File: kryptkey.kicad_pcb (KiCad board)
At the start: 2 copper layers, 34 parts, among them J1 Conn_01x04_Pin, J2 Conn_01x04_Pin, P1 USB_C_Plug, SW4 SW_SPDT, U1 AMS1117-3.3, U2 STM32F103C8T6, Y1 16MHz

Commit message: worked on board layout
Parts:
- removed P1: USB_C_Plug, Connector_USB:USB_C_Plug_Molex_105444
- removed the R2 at (159.2, 77.5)
- added P2: USB_C_Plug_USB2.0, Connector_USB:USB_C_Plug_JAE_DX07P024AJ1, B.Cu at (155.6, 85.0)
- added SW1: SW_Push, Button_Switch_SMD:SW_SPST_B3U-1000P, F.Cu at (145.7, 118.2)
- added SW2: SW_Push, Button_Switch_SMD:SW_SPST_B3U-1000P, F.Cu at (155.7, 117.8)
- added SW3: SW_Push, Button_Switch_SMD:SW_SPST_B3U-1000P, F.Cu at (164.2, 118.0)
- FB1: footprint Inductor_SMD:L_12x12mm_H8mm -> Inductor_SMD:L_0603_1608Metric
- H1, H2, H3, H4: footprint MountingHole:MountingHole_2.5mm -> MountingHole:MountingHole_2.7mm_M2.5
- J2: footprint Connector_PinHeader_2.54mm:PinHeader_1x04_P2.54mm_Vertical -> Connector_PinHeader_2.54mm:PinHeader_1x04_P2.54mm_Horizontal
- SW4: footprint Button_Switch_THT:SW_E-Switch_EG1224_SPDT_Angled -> Button_Switch_THT:SW_E-Switch_EG1271_SPDT
- moved H4 58.8 mm to (165.0, 113.5)
- moved H3 58.6 mm to (165.6, 90.7)
- moved D1 51.0 mm to (167.9, 108.2)
- moved SW4 49.5 mm to (158.1, 115.0), turned to 180 degrees
- moved H2 40.7 mm to (144.8, 113.5)
- moved H1 39.2 mm to (144.8, 90.7)
- moved U1 37.8 mm to (165.2, 102.8)
- moved C10 31.7 mm to (158.1, 108.4), turned to 180 degrees
- moved C13 31.6 mm to (154.1, 109.1), turned to 90 degrees
- moved Y1 28.2 mm to (146.9, 99.1), turned to 180 degrees
- moved R5 27.6 mm to (161.5, 85.8), turned to 180 degrees
- moved C4 26.5 mm to (147.1, 105.2), turned to 180 degrees
- moved R3 23.9 mm to (164.4, 108.3)
- moved R4 22.8 mm to (161.2, 114.6), turned to 90 degrees
- moved U2 21.6 mm to (155.5, 101.1)
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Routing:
- added copper zone on B.Cu, net GND
- added copper zone on F.Cu, net GND
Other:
- board outline added: 30 x 36 mm

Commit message: worked on board layout
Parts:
- moved SW2 0.90 mm to (154.9, 118.2)
- moved SW3 0.31 mm to (164.4, 118.2)
- moved SW1 0.28 mm to (145.4, 118.2)
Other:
- board text added: "4x M2.5"
- board text added: "BOOT0"
- board text added: "SSD1315 OLED"
- board text added: "SWD"
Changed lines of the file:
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@@
 	)
 	(footprint "Button_Switch_SMD:SW_SPST_B3U-1000P"
+		(locked yes)
 		(layer "F.Cu")
-		(at 155.7 117.85)
+		(at 154.875 118.2)
 		(descr "Ultra-small-sized Tactile Switch with High Contact Reliability, Top-actuated Model, without Ground Terminal, without Boss")
 		(tags "Tactile Switch")
 		(property "Reference" "SW2"
-			(at -4.05 -0.1 0)
+			(at -4.2 0.05 0)
 			(layer "F.SilkS")
 			(effects
@@
 			(at 0 -2.5 0)
 			(layer "F.Fab")
+			(hide yes)
 			(effects
 				(font
@@
 		(tags "SMD SMT crystal")
 		(property "Reference" "Y1"
-			(at 2.9625 1.7625 360)
+			(at 2.4125 -2.5375 360)
 			(layer "F.SilkS")
 			(effects
@@
 		(tags "Through hole angled pin header THT 1x04 2.54mm single row")
 		(property "Reference" "J2"
-			(at 0.95 -2.73 180)
+			(at 1.3 -2.68 180)
 			(layer "F.SilkS")
 			(effects
@@
 			(at 0.55 1.5 0)
 			(layer "F.Fab")
+			(hide yes)
 			(effects
 				(font
@@
 	)
 	(footprint "Button_Switch_SMD:SW_SPST_B3U-1000P"
+		(locked yes)
 		(layer "F.Cu")
-		(at 164.2 117.95)
+		(at 164.375 118.2)
 		(descr "Ultra-small-sized Tactile Switch with High Contact Reliability, Top-actuated Model, without Ground Terminal, without Boss")
 		(tags "Tactile Switch")
 		(property "Reference" "SW3"
-			(at 4 -0.05 0)
+			(at -4.05 0.1 0)
 			(layer "F.SilkS")
 			(effects
@@
 		)
 		(fp_text user "${REFERENCE}"
-			(at 4 -0.05 0)
+			(at -4.1 0.15 0)
 			(layer "F.Fab")
+			(hide yes)
 			(effects
 				(font
@@
 	)
 	(footprint "Button_Switch_SMD:SW_SPST_B3U-1000P"
+		(locked yes)
 		(layer "F.Cu")
-		(at 145.65 118.2)
+		(at 145.375 118.2)
 		(descr "Ultra-small-sized Tactile Switch with High Contact Reliability, Top-actuated Model, without Ground Terminal, without Boss")
 		(tags "Tactile Switch")
@@
 		(layer "Edge.Cuts")
 	)
+	(gr_text "SSD1315 OLED\n\n"
+		(at 149 94.25 0)
+		(layer "F.SilkS")
+		(effects
+			(font
+				(size 1 1)
+				(thickness 0.25)
+				(bold yes)
+			)
+			(justify left bottom)
+		)
+	)
+	(gr_text "SWD"
+		(at 141 97.9 0)
+		(layer "F.SilkS")
+		(effects
+			(font
+				(size 1 1)
+				(thickness 0.125)
+			)
+			(justify left bottom)
+		)
+	)
+	(gr_text "4x M2.5"
+		(at 140.05 85.55 0)
+		(layer "F.SilkS")
+		(effects
+			(font
+				(size 1 1)
+				(thickness 0.125)
+			)
+			(justify left bottom)
+		)
+	)
+	(gr_text "BOOT0"
+		(at 146.05 112.35 0)
+		(layer "F.SilkS")
+		(effects
+			(font
+				(size 1 1)
+				(thickness 0.125)
+			)
+			(justify left bottom)
+		)
+	)
 	(segment

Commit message: first pass routing
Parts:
- removed P2: USB_C_Plug_USB2.0, Connector_USB:USB_C_Plug_JAE_DX07P024AJ1
- added J3: USB4155-03-C_REVA, USB4155-03-C_REVA:GCT_USB4155-03-C_REVA, F.Cu at (155.6, 85.2)
- moved R5 9.88 mm to (162.2, 95.6)
- moved R2 3.58 mm to (155.4, 93.2)
- moved R1 3.55 mm to (155.4, 94.8)
- moved C8 2.41 mm to (159.8, 95.8)
- moved C3 1.85 mm to (152.0, 93.5)
- moved C6 1.85 mm to (152.0, 95.2)
- moved C9 1.68 mm to (149.3, 95.7)
- moved R3 1.20 mm to (162.2, 97.2), turned to 0 degrees
- moved R3 1.10 mm to (164.4, 109.5)
- moved D1 1.10 mm to (167.9, 109.3)
- moved U1 1.10 mm to (165.2, 103.8)
- moved R6 0.55 mm to (149.7, 85.5)
- moved C7 0.24 mm to (147.1, 101.8)
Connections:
- R5 pad 1: +3.3V -> /USB_D+
- R5 pad 2: /USB_D+ -> +3.3V
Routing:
- net +3.3V: track 0.00 -> 132.0 mm, vias 0 -> 6
- net GND: track 0.00 -> 71.3 mm, vias 0 -> 17
- net VBUS: track 0.00 -> 37.5 mm, vias 0 -> 5
- net /USB_D-: track 0.00 -> 22.4 mm
- net /USB_D+: track 0.00 -> 21.9 mm
- net /UI_DOWN_BUTTON: track 0.00 -> 20.0 mm
- net /SWCLK: track 0.00 -> 20.0 mm, vias 0 -> 2
- net /UI_UP_BUTTON: track 0.00 -> 19.6 mm, vias 0 -> 2
- net /SWDIO: track 0.00 -> 19.5 mm, vias 0 -> 2
- net /BOOT0: track 0.00 -> 19.5 mm
- net +3.3V_A: track 0.00 -> 17.9 mm, vias 0 -> 4
- net /UI_ENTER_BUTTON: track 0.00 -> 15.9 mm
- net /I2C1_SDA_OLED: track 0.00 -> 10.9 mm, vias 0 -> 2
- net /NRST: track 0.00 -> 10.7 mm
- net /I2C1_SCL_OLED: track 0.00 -> 10.2 mm, vias 0 -> 2
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- removed copper zone on F.Cu, net GND
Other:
- board size 30 x 36 mm -> 30 x 36.1 mm
- board text added: "A.Q.Snyder"
- board text added: "JLCJLCJLC"
- board text added: "Kryptkey"
- board text added: "M2.5"
- board text added: "Rev: v0.1"
- board text removed: "4x M2.5"

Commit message: error free DRC
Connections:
- net +3.3V renamed +3V3
- net +3.3V_A renamed +3V3_A

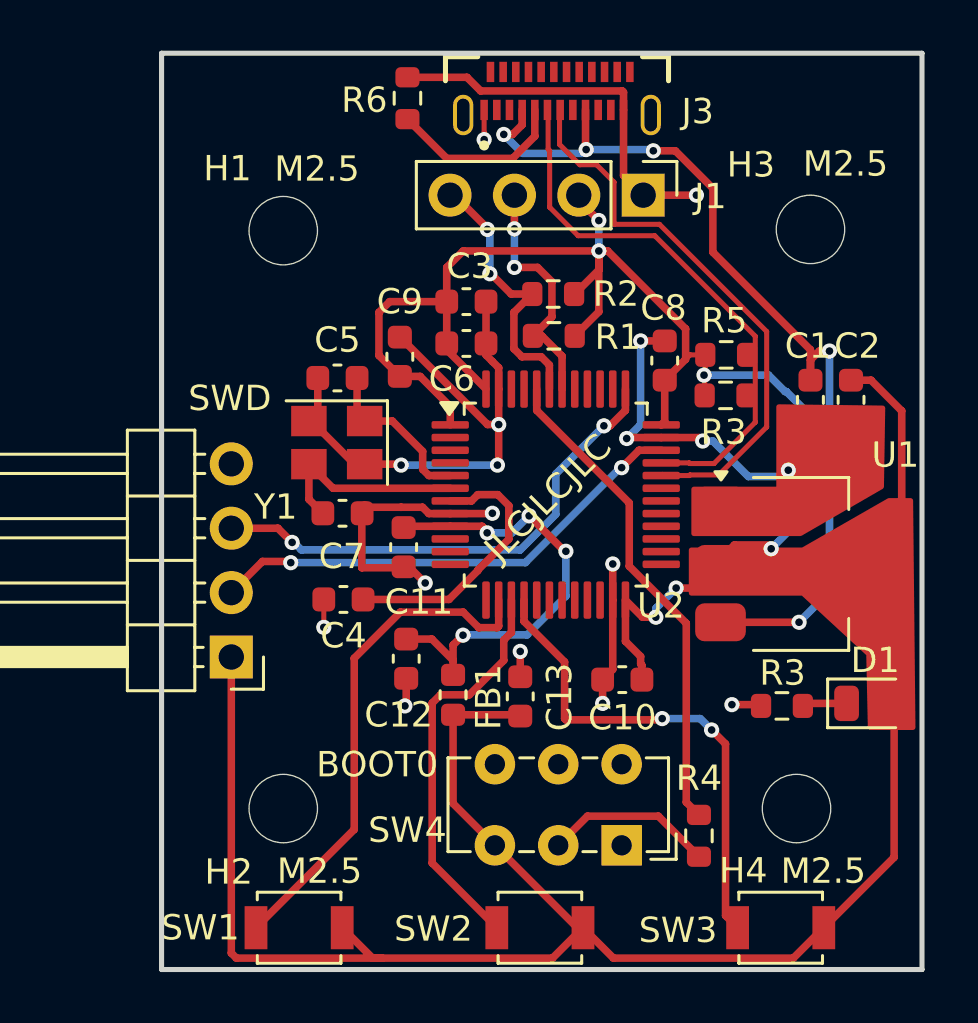
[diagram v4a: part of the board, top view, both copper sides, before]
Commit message: final mounting hole possitions and flipped UI botton side
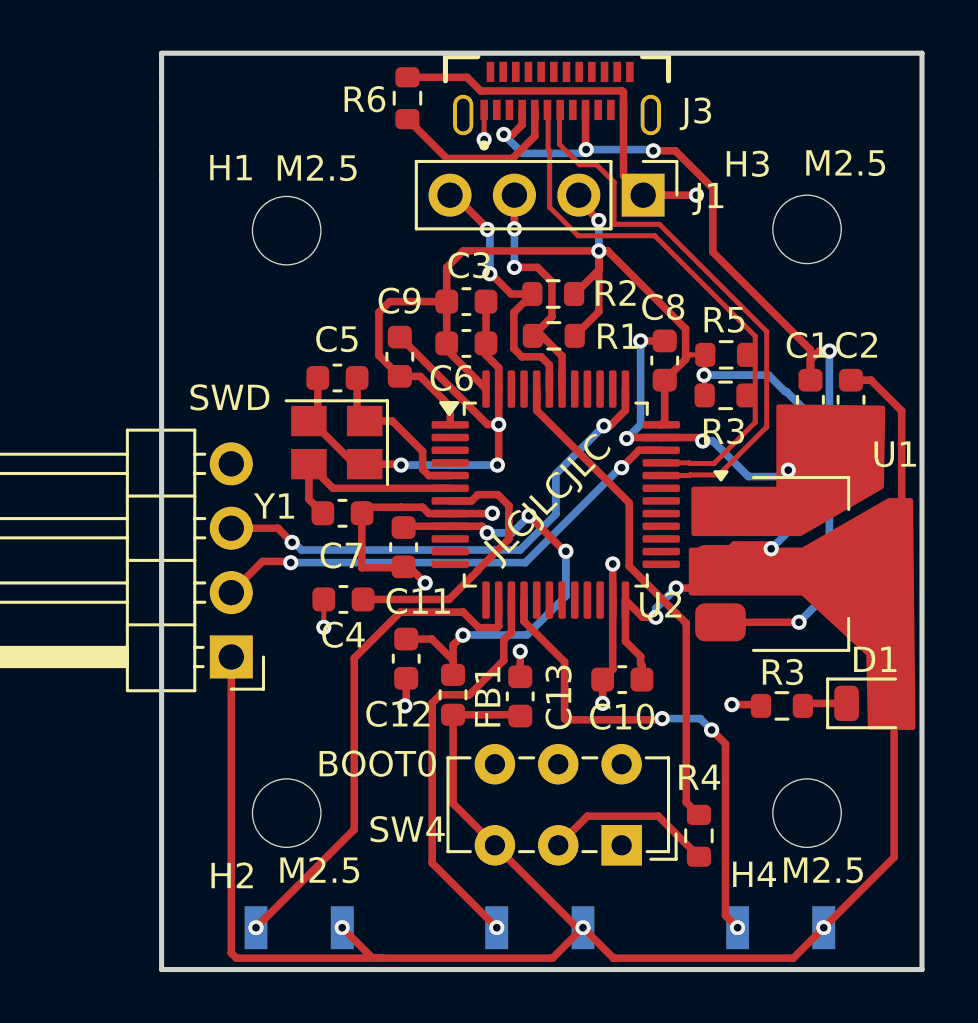
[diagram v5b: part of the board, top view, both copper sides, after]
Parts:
- SW1, SW2, SW3: moved to B.Cu
- moved H4 0.45 mm to (165.4, 113.7)
- moved H2 0.23 mm to (144.9, 113.7)
- moved H3 0.14 mm to (165.4, 90.7)
- moved H1 0.13 mm to (144.9, 90.7)
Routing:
- net /UI_UP_BUTTON: vias 2 -> 3
- net /UI_ENTER_BUTTON: vias 0 -> 1
- net /UI_DOWN_BUTTON: vias 0 -> 1
- net +3V3: vias 6 -> 9

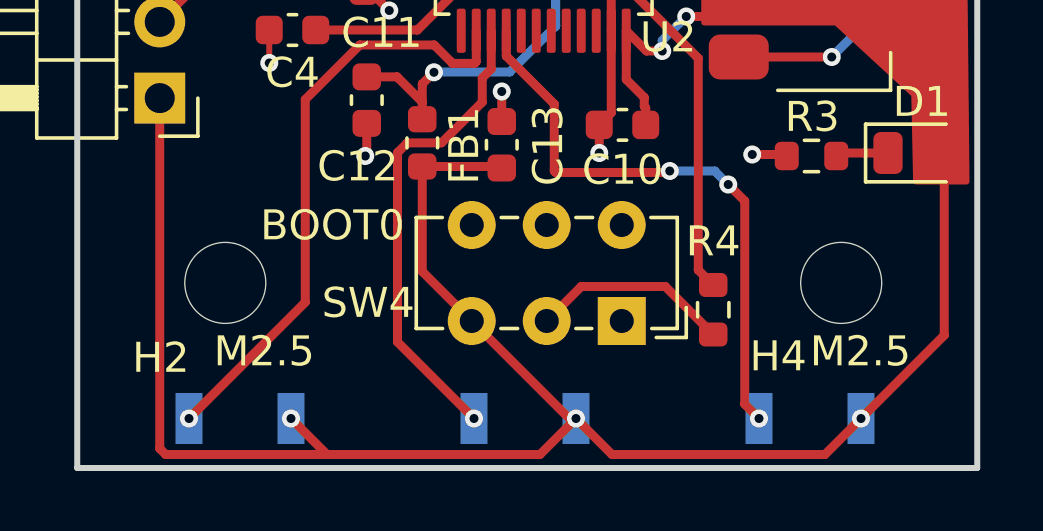
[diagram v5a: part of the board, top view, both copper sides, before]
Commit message: spaced UI button vias off of the pads for solder drainage prevention
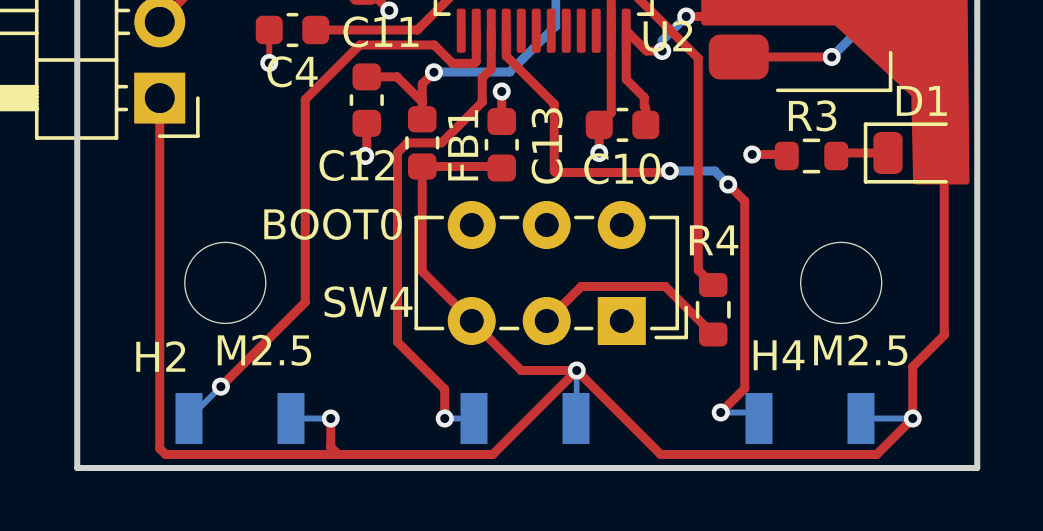
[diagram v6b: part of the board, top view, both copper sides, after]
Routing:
- net +3V3: track 132.0 -> 137.6 mm
- net /UI_UP_BUTTON: track 19.6 -> 20.9 mm
- net /UI_ENTER_BUTTON: track 15.9 -> 16.5 mm

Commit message: v0.1 jlcpcb production order
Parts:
- moved C1 56.3 mm to (118.7, 66.1)
- moved C8 56.3 mm to (113.0, 64.6)
- moved J3 56.3 mm to (108.7, 53.9)
- moved R1 56.3 mm to (108.6, 63.6)
- moved R3 56.3 mm to (117.6, 78.2)
- moved Y1 56.3 mm to (100.0, 67.8)
- moved C10 56.3 mm to (111.3, 77.2)
- moved C11 56.3 mm to (102.7, 71.9)
- moved C12 56.3 mm to (102.8, 76.3)
- moved C13 56.3 mm to (107.3, 77.8)
- moved C2 56.3 mm to (120.3, 66.1)
- moved C3 56.3 mm to (105.1, 62.3)
- moved C4 56.3 mm to (100.3, 74.0)
- moved C6 56.3 mm to (105.1, 63.9)
- moved C7 56.3 mm to (100.3, 70.6)
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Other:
- board size 30 x 36.1 mm -> 30 x 36.2 mm
